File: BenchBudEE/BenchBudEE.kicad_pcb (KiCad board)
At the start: 4 copper layers, 165.1 x 63.5 mm, 58 parts, among them K1 1461069-5, P1 24 pin Mini-fit Jr, P2 CONN_3X2, P3 CONN_2, P4 12 pin terminal block, P5 3 Pin TB, Q1 2N3904, U1 LTV-816S, U2 MCP3901, U3 LMT84, U4 OPA4170

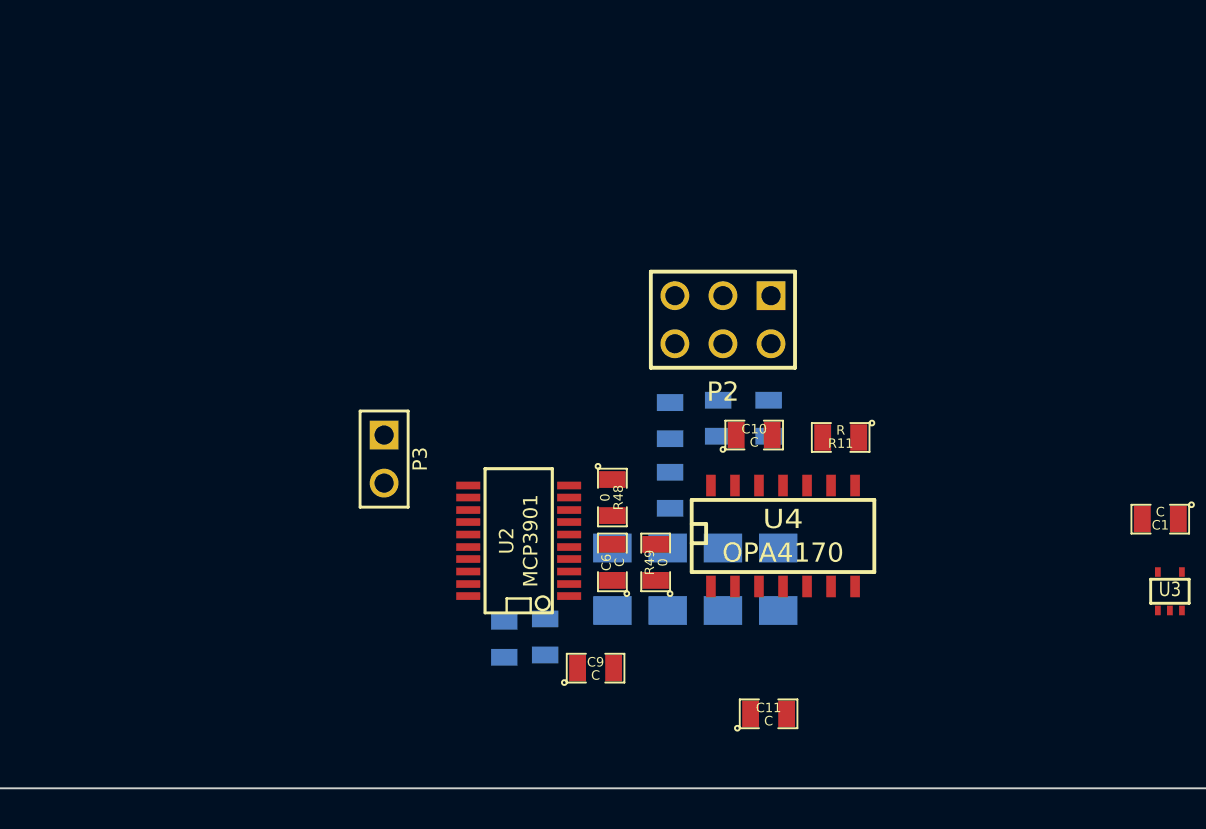
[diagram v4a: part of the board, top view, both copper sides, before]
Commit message: Associating and Placing the Power protection module
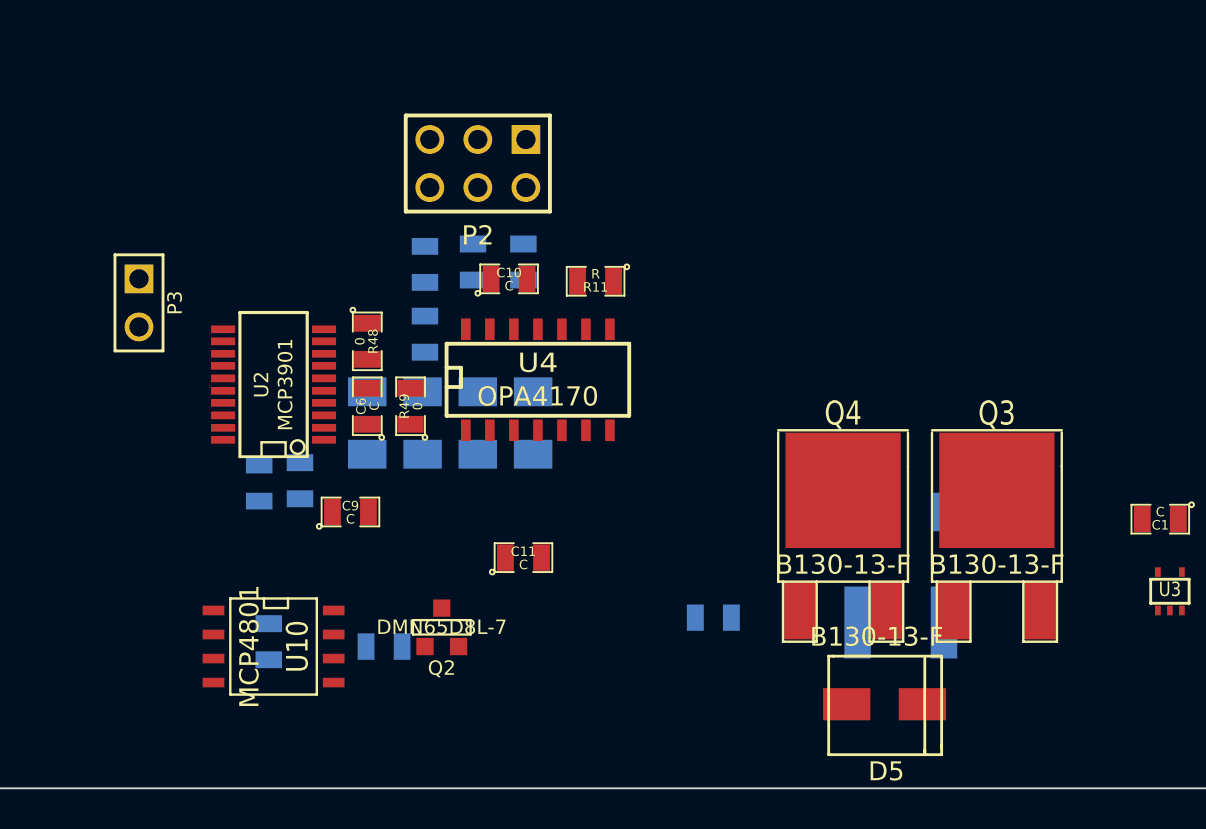
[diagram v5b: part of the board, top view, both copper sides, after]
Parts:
- added C12: C, SM0805, B.Cu at (226.3, 153.8)
- added C13: C, SM0805, B.Cu at (249.8, 152.5)
- added D5: B130-13-F, SMA, F.Cu at (260.9, 157.1)
- added Q2: DMN65D8L-7, SOT23GDS, F.Cu at (235.5, 153.0)
- added Q3: B130-13-F, DPAK2, F.Cu at (264.8, 152.1)
- added Q4: B130-13-F, DPAK2, F.Cu at (256.7, 152.1)
- added R42: R, SM0805, B.Cu at (232.4, 154.1)
- added R43: R, SM1206, B.Cu at (260.5, 146.9)
- added TH5: MINISMDCO50F-2, SM1812, B.Cu at (259.7, 152.8)
- added U10: MCP4801, SO8N, F.Cu at (226.6, 154.1)
- moved P3 15.4 mm to (219.5, 135.9)
- moved C6 15.4 mm to (231.5, 141.4)
- moved C8 15.4 mm to (228.0, 145.3)
- moved C9 15.4 mm to (230.6, 146.9)
- moved P2 15.4 mm to (237.4, 128.5)
- moved R10 15.4 mm to (240.3, 142.2)
- moved R11 15.4 mm to (243.6, 134.7)
- moved R13 15.4 mm to (234.6, 137.5)
- moved R44 15.4 mm to (234.6, 133.9)
- moved R48 15.4 mm to (231.5, 137.9)
- moved R49 15.4 mm to (233.8, 141.4)
- moved R7 15.4 mm to (231.5, 142.2)
- moved R9 15.4 mm to (237.4, 142.2)
- moved C10 15.4 mm to (239.0, 134.6)
- moved C11 15.4 mm to (239.8, 149.4)
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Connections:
- net /Arduino/ADC_CS_N renamed /Arduino/~ADC_CS
- ARD1 pad 13: (no net) -> N-0000049
- ARD1 pad 14: (no net) -> N-0000048

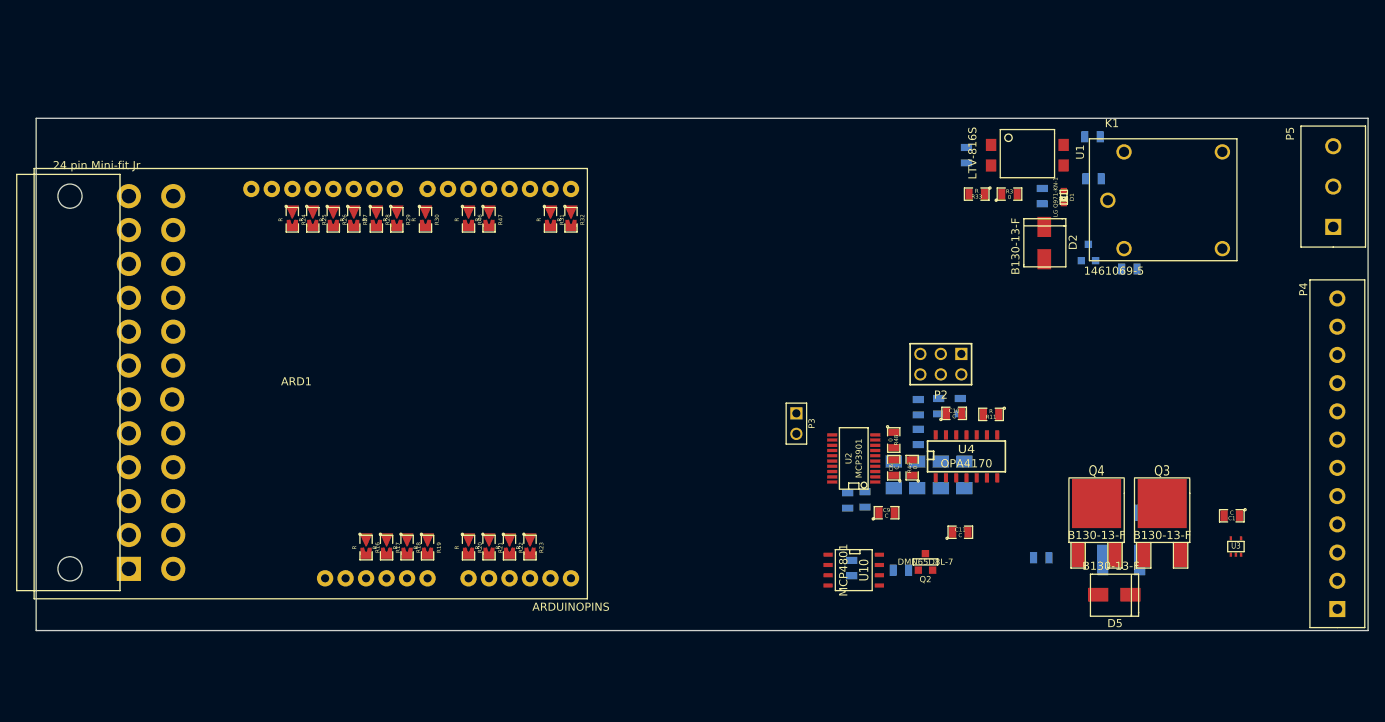
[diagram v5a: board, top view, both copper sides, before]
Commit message: Associating and Placing the Power Modification Module
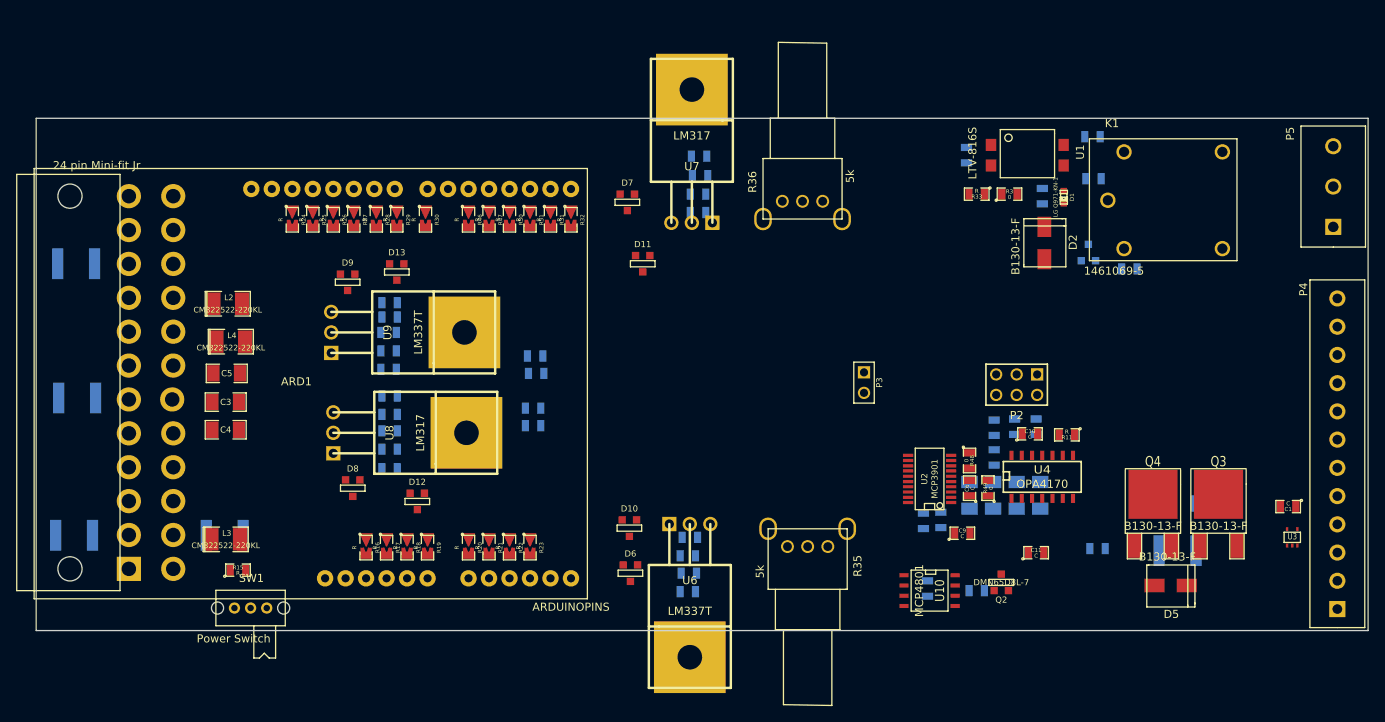
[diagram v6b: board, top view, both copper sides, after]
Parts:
- added C14: C, SM0805, B.Cu at (206.2, 150.0)
- added C15: C, SM0805, B.Cu at (207.3, 109.7)
- added C16: C, SM0805, B.Cu at (169.0, 141.5)
- added C17: C, SM0805, B.Cu at (169.0, 120.9)
- added C18: C, SM0805, B.Cu at (206.0, 156.7)
- added C19: C, SM0805, B.Cu at (207.3, 107.4)
- added C20: C, SM0805, B.Cu at (169.0, 132.5)
- added C21: C, SM0805, B.Cu at (168.9, 129.2)
- added C22: C, SM0805, B.Cu at (206.1, 154.4)
- added C23: C, SM0805, B.Cu at (207.4, 102.7)
- added C24: C, SM0805, B.Cu at (169.0, 122.7)
- added C25: C, SM0805, B.Cu at (169.0, 136.8)
- added C3: C, SM1206, F.Cu at (148.7, 133.2)
- added C4: C, SM1206, F.Cu at (148.7, 136.7)
- added C5: C, SM1206, F.Cu at (148.8, 129.7)
- added D10: MMBD914-7-F, SOT23-DIODE, F.Cu at (198.8, 148.8)
- added D11: MMBD914-7-F, SOT23-DIODE, F.Cu at (200.4, 116.1)
- added D12: MMBD914-7-F, SOT23-DIODE, F.Cu at (172.5, 145.5)
- added D13: MMBD914-7-F, SOT23-DIODE, F.Cu at (169.9, 117.1)
- added D6: MMBD914-7-F, SOT23-DIODE, F.Cu at (198.9, 154.4)
- added D7: MMBD914-7-F, SOT23-DIODE, F.Cu at (198.5, 108.5)
- added D8: MMBD914-7-F, SOT23-DIODE, F.Cu at (164.5, 143.9)
- added D9: MMBD914-7-F, SOT23-DIODE, F.Cu at (163.8, 118.4)
- added L2: CM322522-220KL, SM1210L, F.Cu at (149.0, 121.0)
- added L3: CM322522-220KL, SM1210L, F.Cu at (148.7, 150.2)
- added L4: CM322522-220KL, SM1210L, F.Cu at (149.4, 125.7)
- added R15: R, SM0805, F.Cu at (150.2, 154.1)
- added R34: 715, SM0805, B.Cu at (206.0, 152.3)
- added R35: 5k, EVUE3K, F.Cu at (220.9, 151.1)
- added R36: 5k, EVUE3K, F.Cu at (220.2, 108.3)
- added R37: 715, SM0805, B.Cu at (207.5, 105.2)
- added R38: R, SM0805, B.Cu at (187.1, 127.5)
- added R39: R, SM0805, B.Cu at (187.2, 129.7)
- added R40: R, SM0805, B.Cu at (186.8, 134.0)
- added R41: R, SM0805, B.Cu at (186.8, 136.1)
- added R50: R, SM0805-blob, F.Cu at (183.9, 110.6)
- added R51: R, SM0805-blob, F.Cu at (186.4, 110.6)
- added R52: R, SM0805, B.Cu at (169.0, 134.7)
- added R53: R, SM0805, B.Cu at (169.0, 139.1)
- added R54: R, SM0805, B.Cu at (168.9, 126.9)
- added R55: R, SM0805, B.Cu at (168.9, 124.6)
- added SW1: Power Switch, BB_Switch, F.Cu at (147.7, 158.8)
- added TH1: MINISMDC050F-2, SM1812, B.Cu at (129.9, 149.7)
- added TH2: MINISMDC050F-2, SM1812, B.Cu at (130.3, 132.7)
- added TH3: MINISMDC050F-2, SM1812, B.Cu at (130.2, 116.1)
- added TH4: MINISMDC050F-2, SM1812, B.Cu at (148.6, 149.7)
- added U6: LM337T, TO220, F.Cu at (206.2, 148.3)
- added U7: LM317, TO220, F.Cu at (206.5, 111.0)
- added U8: LM317, TO220, F.Cu at (162.1, 137.0)
- added U9: LM337T, TO220, F.Cu at (161.8, 124.6)
- moved P3 9.80 mm to (227.8, 130.8)
- moved C6 9.74 mm to (240.9, 143.9)
- moved R13 9.74 mm to (244.0, 140.1)
- moved R44 9.74 mm to (244.0, 136.4)
- moved R48 9.74 mm to (240.9, 140.5)
- moved R49 9.74 mm to (243.2, 143.9)
- moved R7 9.74 mm to (240.9, 144.8)
- moved C7 9.74 mm to (235.2, 148.0)
- moved C9 9.74 mm to (240.0, 149.5)
- moved R42 9.74 mm to (241.8, 156.6)
- moved U10 9.74 mm to (236.0, 156.6)
- moved C10 9.74 mm to (248.4, 137.2)
- moved C11 9.74 mm to (249.2, 151.9)
- moved C12 9.74 mm to (235.7, 156.3)
- moved C8 9.74 mm to (237.4, 147.8)
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
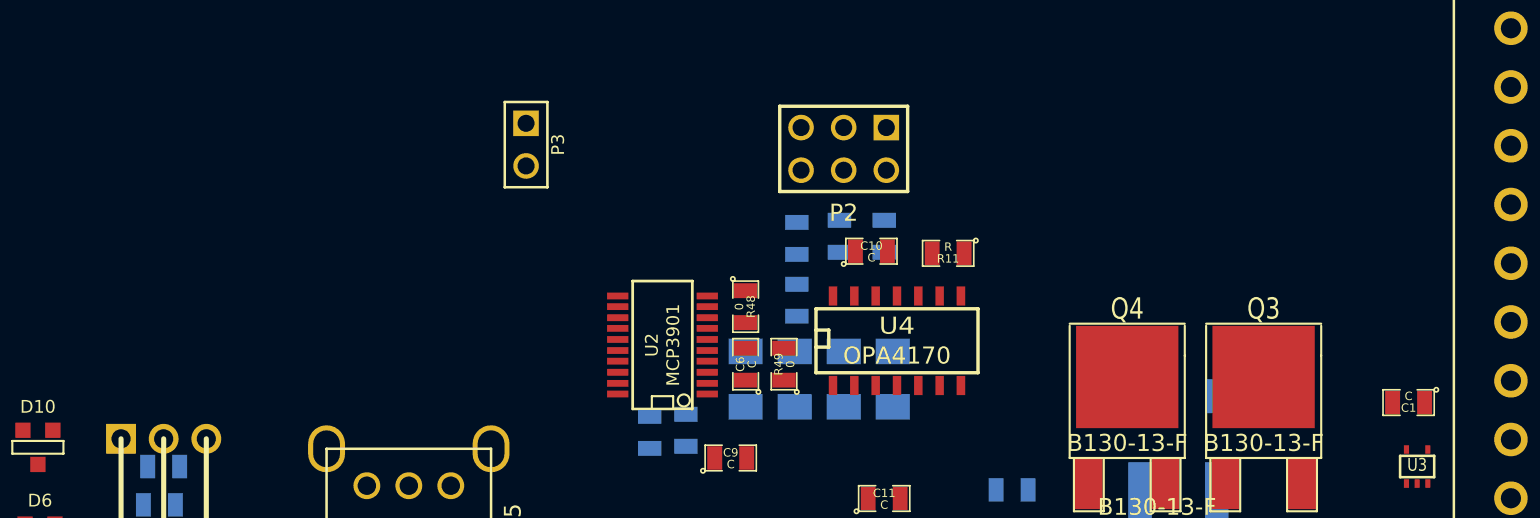
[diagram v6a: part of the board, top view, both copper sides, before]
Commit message: Associating and Placing the LED Driver Module
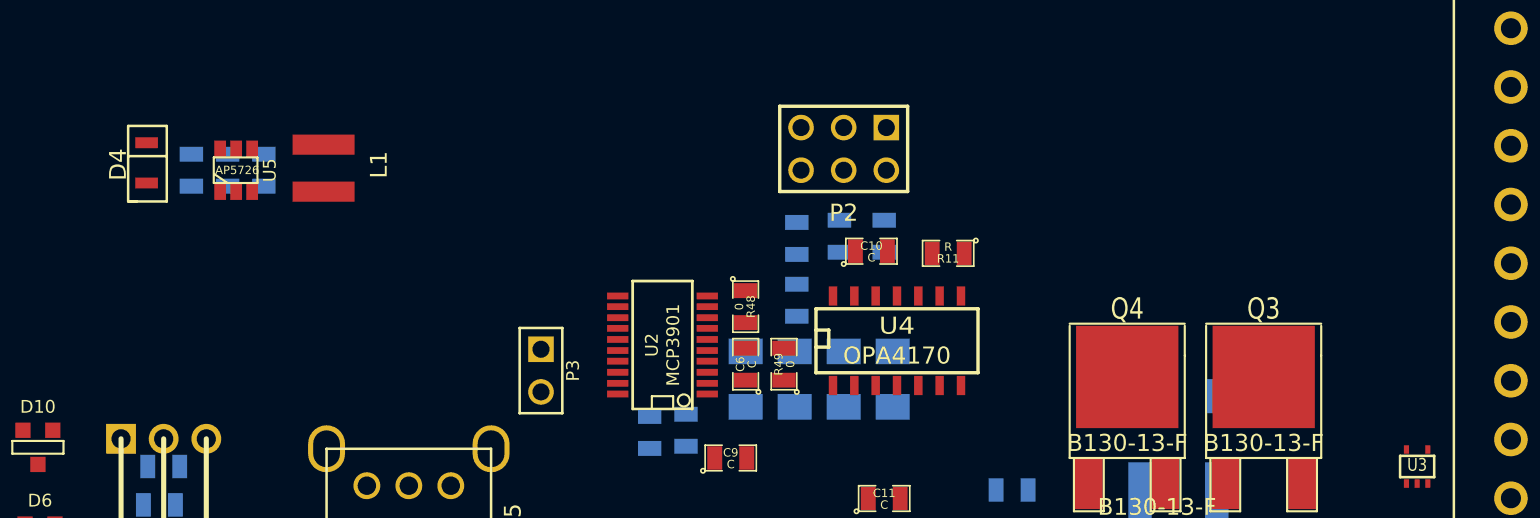
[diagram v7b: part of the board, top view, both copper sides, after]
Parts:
- added C2: 1u, SM0805, B.Cu at (210.1, 132.3)
- added D4: B0540WS-7, SOD-323, F.Cu at (205.2, 133.1)
- added L1: 22u, NR4012, F.Cu at (215.8, 130.8)
- added R14: 15, SM0805, B.Cu at (212.2, 132.3)
- added U5: AP5726, SOT23_6, F.Cu at (210.6, 132.3)
- C1: value C -> 1u; moved to B.Cu
- moved C1 73.8 mm to (207.9, 132.3), turned to 270 degrees
- moved P3 13.5 mm to (228.7, 144.3)

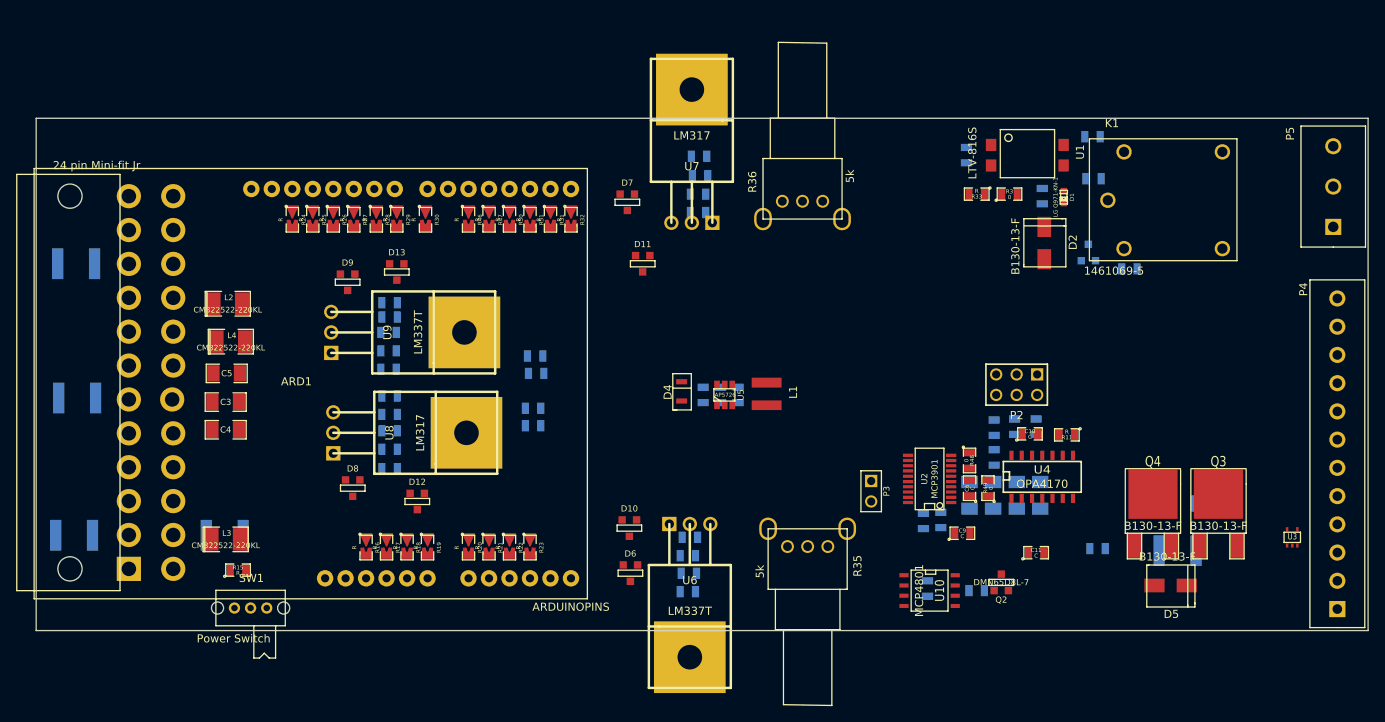
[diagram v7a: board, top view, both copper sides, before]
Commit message: Finalizing the system part placement
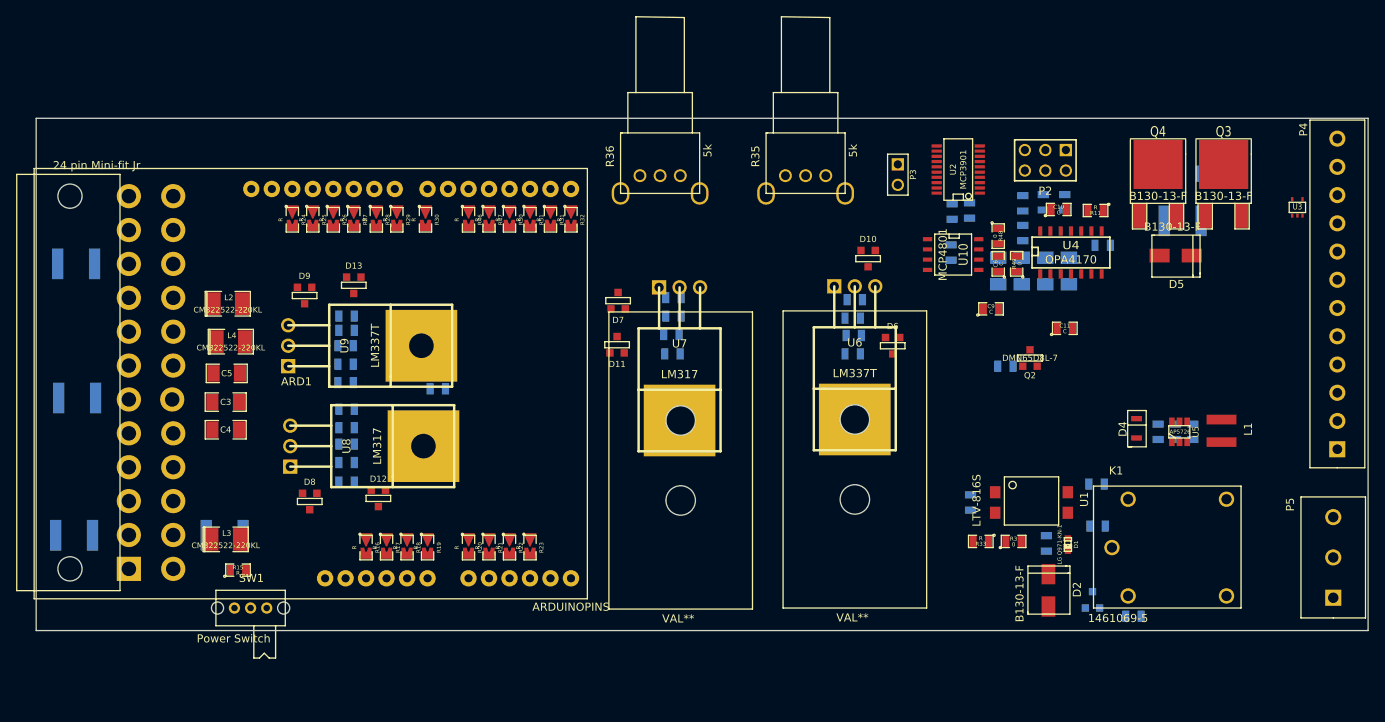
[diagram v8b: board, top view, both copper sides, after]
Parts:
- added V2006B: VAL**, V2006B, F.Cu at (217.8, 158.8)
- added V2006B: VAL**, V2006B, F.Cu at (196.2, 158.9)
- moved C2 56.6 mm to (266.4, 136.9)
- moved D4 56.6 mm to (261.6, 137.7)
- moved L1 56.6 mm to (272.2, 135.4)
- moved R14 56.6 mm to (268.6, 136.9)
- moved U5 56.6 mm to (267.0, 136.9)
- moved C1 56.6 mm to (264.3, 136.9)
- moved R35 46.0 mm to (220.6, 105.2), turned to 90 degrees
- moved P5 46.0 mm to (286.0, 157.5)
- moved D10 44.6 mm to (228.3, 115.4)
- moved D1 43.1 mm to (253.1, 150.9)
- moved K1 43.1 mm to (258.6, 151.3)
- moved Q1 43.1 mm to (256.2, 157.7)
- moved R1 43.1 mm to (241.0, 145.7)
- moved R3 43.1 mm to (246.4, 150.5)
- moved R33 43.1 mm to (242.3, 150.5)
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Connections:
- P4 pad 10: (no net) -> /Fan/FAN_OUT-
- P4 pad 11: /LED_Driver/LED_STRING+ -> /Thermocouple/TC IN +
- P4 pad 12: /LED_Driver/LED_STRING- -> /Thermocouple/TC IN -
- P4 pad 6: /Fan/FAN_OUT+ -> /LED_Driver/LED_STRING+
- P4 pad 7: /Fan/FAN_OUT- -> /LED_Driver/LED_STRING-
- P4 pad 9: (no net) -> /Fan/FAN_OUT+
- U4 pad 10: (no net) -> /Thermocouple/TC IN +
- U4 pad 12: (no net) -> /Thermocouple/TC IN -
